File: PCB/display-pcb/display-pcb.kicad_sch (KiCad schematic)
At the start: 7 parts, among them J1 B6B-XH-A, J2 B8B-XH-A, SW1 PTS645SL50-2 LFS, SW2 PTS645SL50-2 LFS, SW3 PTS645SL50-2 LFS, SW4 PTS645SL50-2 LFS, U1 NHD-C12864A1Z

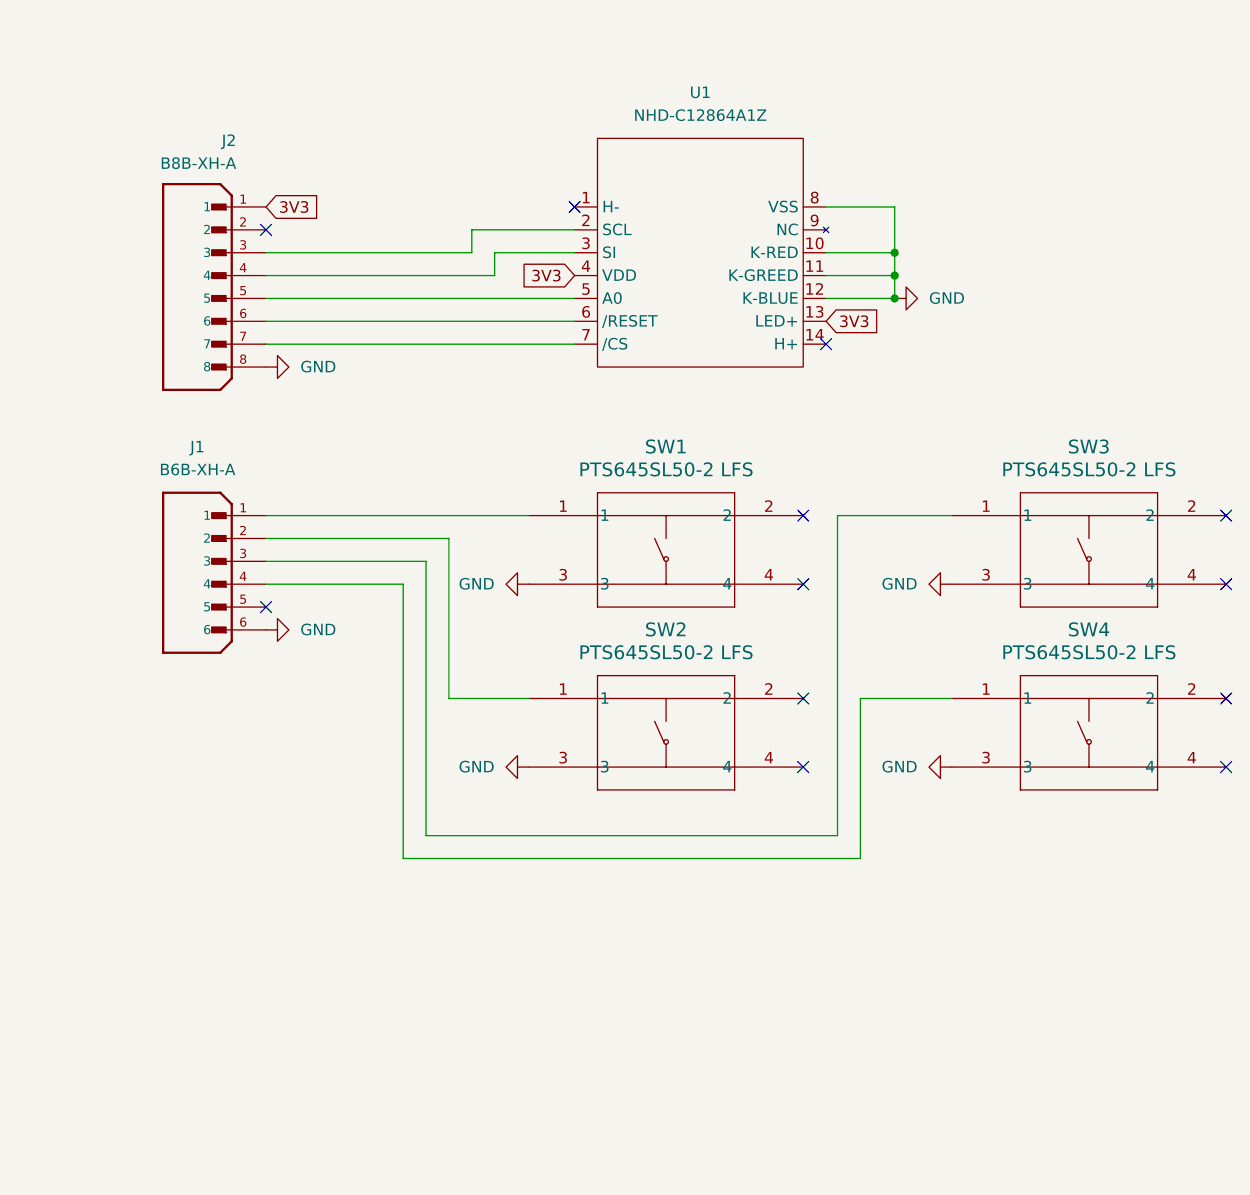
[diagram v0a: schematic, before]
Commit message: changes to display and tube pcb
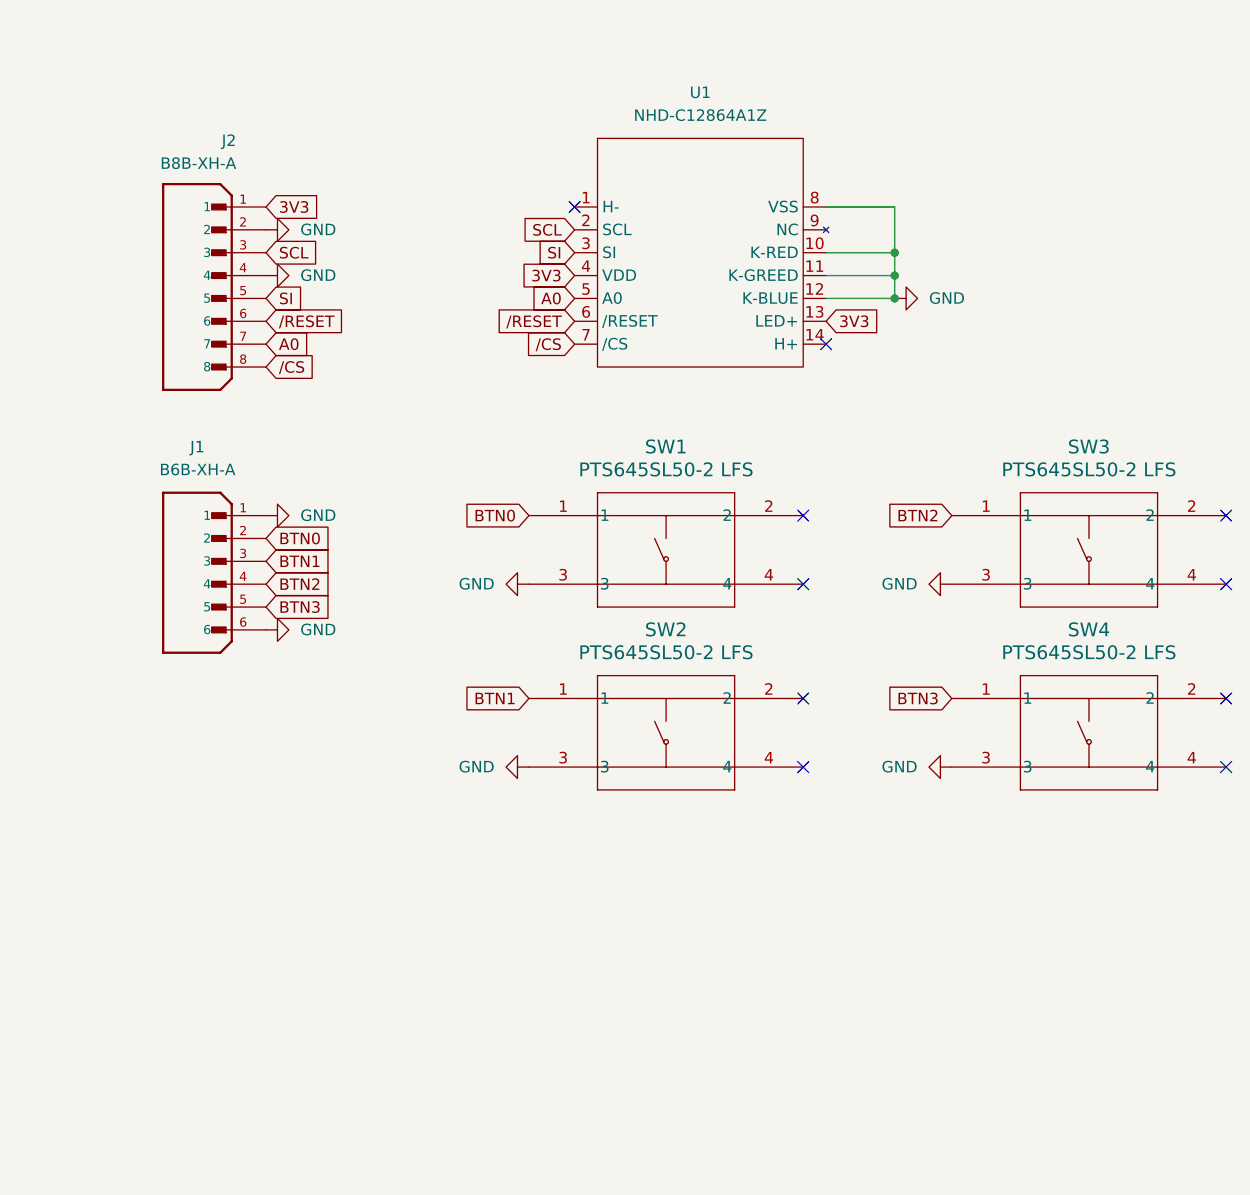
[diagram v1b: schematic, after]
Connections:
- net GND: now also J1.1, J2.2, J2.4; no longer J2.8
- net BTN1: now reaches J1.3
- net BTN1: now also SW2.1; no longer SW3.1
- net BTN0: now reaches SW1.1
- net BTN0: now also J1.2; no longer J1.1
- net BTN2: now reaches J1.4
- net BTN2: now also SW3.1; no longer SW4.1
- net BTN3: now reaches J1.5
- net BTN3: now also SW4.1
- net SCL: now reaches J2.3, U1.2 (SCL)
- net SI: now reaches U1.3 (SI)
- net SI: now also J2.5; no longer J2.4
- net A0: now reaches U1.5 (A0)
- net A0: now also J2.7; no longer J2.5
- net /RESET: now reaches J2.6, U1.6 (/RESET)
- net /CS: now reaches U1.7 (/CS)
- net /CS: now also J2.8; no longer J2.7
- no-connect marks 12 -> 10

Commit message: pcb silkscreens mostly
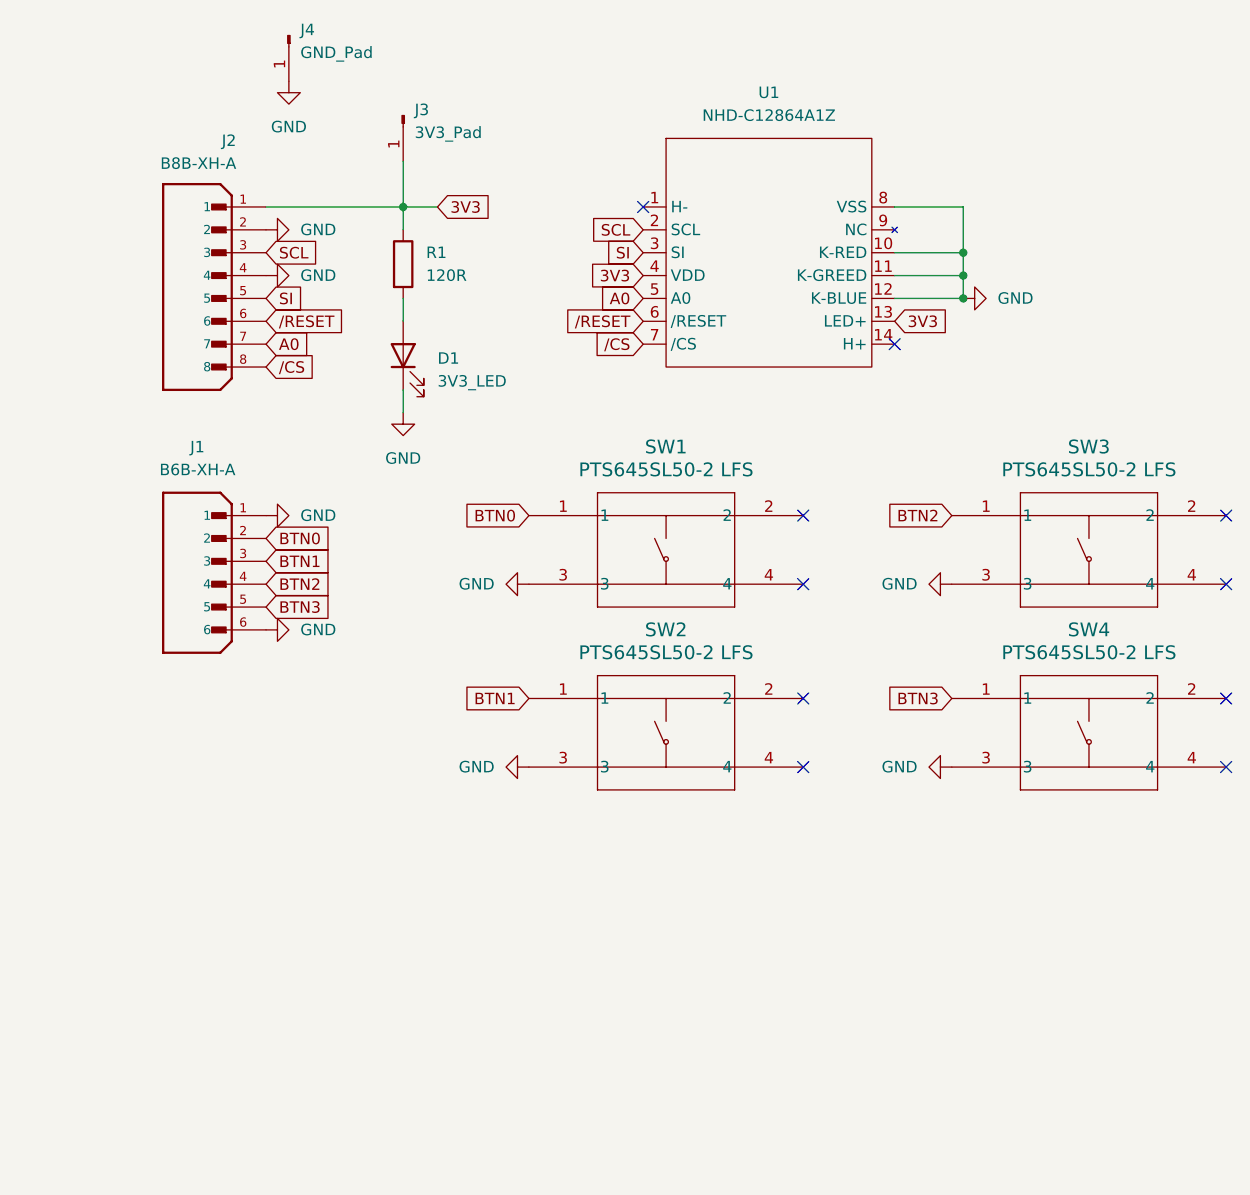
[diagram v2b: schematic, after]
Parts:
- added D1: 3V3_LED, LED_THT:LED_D3.0mm, symbol Device:LED
- added J3: 3V3_Pad, Connector_Wire:SolderWirePad_1x01_SMD_2x4mm, symbol Connector:Conn_01x01_Pin
- added J4: GND_Pad, Connector_Wire:SolderWirePad_1x01_SMD_2x4mm, symbol Connector:Conn_01x01_Pin
- added R1: 120R, 10k-resistor:YAG_MF25_YAG, symbol Device:R
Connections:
- net 3V3: now also J3.1 (Pin_1), R1.1
- net GND: now also D1.1 (K), J4.1 (Pin_1)
- new net: D1.2 (A), R1.2
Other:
- moved on the sheet: U1

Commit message: pcb stuff i forget
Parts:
- removed J3: 3V3_Pad, Connector_Wire:SolderWirePad_1x01_SMD_2x4mm, symbol Connector:Conn_01x01_Pin
- removed J4: GND_Pad, Connector_Wire:SolderWirePad_1x01_SMD_2x4mm, symbol Connector:Conn_01x01_Pin
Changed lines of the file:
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@@
-	(wire
-		(pts
-			(xy 105.41 50.8) (xy 105.41 55.88)
-		)
-		(stroke
-			(width 0)
-			(type default)
-		)
-	)
 	(wire
 		(pts
@@
 	(symbol
 		(lib_id "power:GND")
-		(at 92.71 41.91 0)
-		(unit 1)
-		(exclude_from_sim no)
-		(in_bom yes)
-		(on_board yes)
-		(dnp no)
-		(fields_autoplaced yes)
-		(property "Reference" "#PWR011"
-			(at 92.71 48.26 0)
-			(effects
-				(font
-					(size 1.27 1.27)
-				)
-				(hide yes)
-			)
-		)
-		(property "Value" "GND"
-			(at 92.71 46.99 0)
-			(effects
-				(font
-					(size 1.27 1.27)
-				)
-			)
-		)
-		(property "Footprint" ""
-			(at 92.71 41.91 0)
-			(effects
-				(font
-					(size 1.27 1.27)
-				)
-				(hide yes)
-			)
-		)
-		(property "Datasheet" ""
-			(at 92.71 41.91 0)
-			(effects
-				(font
-					(size 1.27 1.27)
-				)
-				(hide yes)
-			)
-		)
-		(property "Description" "Power symbol creates a global label with name \"GND\" , ground"
-			(at 92.71 41.91 0)
-			(effects
-				(font
-					(size 1.27 1.27)
-				)
-				(hide yes)
-			)
-		)
-		(pin "1"
-		)
-		(instances
-			(project "display-pcb"
-				(path "/35f2d1cd-48fc-4b0c-8241-cdc4ba0a0621"
-					(reference "#PWR011")
-					(unit 1)
-				)
-			)
-		)
-	)
-	(symbol
-		(lib_id "power:GND")
 		(at 166.37 118.11 270)
 		(unit 1)
@@
 	)
 	(symbol
-		(lib_id "Connector:Conn_01x01_Pin")
-		(at 92.71 36.83 270)
-		(unit 1)
-		(exclude_from_sim no)
-		(in_bom yes)
-		(on_board yes)
-		(dnp no)
-		(fields_autoplaced yes)
-		(property "Reference" "J4"
-			(at 93.98 36.1949 90)
-			(effects
-				(font
-					(size 1.27 1.27)
-				)
-				(justify left)
-			)
-		)
-		(property "Value" "GND_Pad"
-			(at 93.98 38.7349 90)
-			(effects
-				(font
-					(size 1.27 1.27)
-				)
-				(justify left)
-			)
-		)
-		(property "Footprint" "Connector_Wire:SolderWirePad_1x01_SMD_2x4mm"
-			(at 92.71 36.83 0)
-			(effects
-				(font
-					(size 1.27 1.27)
-				)
-				(hide yes)
-			)
-		)
-		(property "Datasheet" "~"
-			(at 92.71 36.83 0)
-			(effects
-				(font
-					(size 1.27 1.27)
-				)
-				(hide yes)
-			)
-		)
-		(property "Description" "Generic connector, single row, 01x01, script generated"
-			(at 92.71 36.83 0)
-			(effects
-				(font
-					(size 1.27 1.27)
-				)
-				(hide yes)
-			)
-		)
-		(pin "1"
-		)
-		(instances
-			(project "display-pcb"
-				(path "/35f2d1cd-48fc-4b0c-8241-cdc4ba0a0621"
-					(reference "J4")
-					(unit 1)
-				)
-			)
-		)
-	)
-	(symbol
 		(lib_id "2026-01-20_18-23-47:PTS645SL50-2_LFS")
 		(at 119.38 110.49 0)
@@
 					(unit 1)
 				)
-			)
-		)
-	)
-	(symbol
-		(lib_id "Connector:Conn_01x01_Pin")
-		(at 105.41 45.72 270)
-		(unit 1)
-		(exclude_from_sim no)
-		(in_bom yes)
-		(on_board yes)
-		(dnp no)
-		(fields_autoplaced yes)
-		(property "Reference" "J3"
-			(at 106.68 45.0849 90)
-			(effects
-				(font
-					(size 1.27 1.27)
-				)
-				(justify left)
-			)
-		)
-		(property "Value" "3V3_Pad"
-			(at 106.68 47.6249 90)
-			(effects
-				(font
-					(size 1.27 1.27)
-				)
-				(justify left)
-			)
-		)
-		(property "Footprint" "Connector_Wire:SolderWirePad_1x01_SMD_2x4mm"
-			(at 105.41 45.72 0)
-			(effects
-				(font
-					(size 1.27 1.27)
-				)
-				(hide yes)
-			)
-		)
-		(property "Datasheet" "~"
-			(at 105.41 45.72 0)
-			(effects
-				(font
-					(size 1.27 1.27)
-				)
-				(hide yes)
-			)
-		)
-		(property "Description" "Generic connector, single row, 01x01, script generated"
-			(at 105.41 45.72 0)
-			(effects
-				(font
-					(size 1.27 1.27)
-				)
-				(hide yes)
-			)
-		)
-		(pin "1"
-		)
-		(instances
-			(project ""
-				(path "/35f2d1cd-48fc-4b0c-8241-cdc4ba0a0621"
-					(reference "J3")
-					(unit 1)
-				)

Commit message: PCB updates
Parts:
- added J3: B8B-XH-A, Connector_JST:JST_XH_B8B-XH-A_1x08_P2.50mm_Vertical, symbol B8B-XH-A:B8B-XH-A
- added U2: ~, microsd:pmod-microsd, symbol microsd-2:pmod-microsd
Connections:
- net A0: now also J2.6; no longer J2.7
- net GND: now also J3.2, J3.5, J3.7, U2.5 (GND)
- net /RESET: now also J2.7; no longer J2.6
- new net SD_3V3: J3.8, U2.6 (VCC)
- new net SD_CSn: J3.1, U2.1 (CSn)
- new net SD_MISO: J3.4, U2.3 (MISO/Data0)
- new net SD_MOSI: J3.3, U2.2 (MOSI/Cmd)
- new net SD_SCK: J3.6, U2.4 (SCK)
- no-connect marks 10 -> 16
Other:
- moved on the sheet: J1, J2

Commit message: pcb finishing touches
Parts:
- J2: value B8B-XH-A -> Display_Header
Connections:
- net A0: now also J2.7; no longer J2.6
- net GND: now also J3.4, J3.8; no longer J3.5, J3.7
- net SD_3V3: now also J3.1; no longer J3.8
- net SD_CSn: now also J3.7; no longer J3.1
- net SD_MISO: now also J3.6; no longer J3.4
- net SD_SCK: now also J3.5; no longer J3.6
- net /RESET: now also J2.6; no longer J2.7
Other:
- moved on the sheet: J3
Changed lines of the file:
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@@
 	(wire
 		(pts
-			(xy 86.36 71.12) (xy 90.17 71.12)
+			(xy 160.02 60.96) (xy 167.64 60.96)
 		)
 		(stroke
@@
 	(wire
 		(pts
-			(xy 86.36 68.58) (xy 90.17 68.58)
+			(xy 105.41 55.88) (xy 105.41 58.42)
 		)
 		(stroke
@@
 	(wire
 		(pts
-			(xy 160.02 60.96) (xy 167.64 60.96)
+			(xy 86.36 55.88) (xy 105.41 55.88)
 		)
 		(stroke
@@
 	(wire
 		(pts
-			(xy 105.41 55.88) (xy 105.41 58.42)
+			(xy 86.36 60.96) (xy 90.17 60.96)
 		)
 		(stroke
@@
 	(wire
 		(pts
-			(xy 86.36 55.88) (xy 105.41 55.88)
+			(xy 167.64 55.88) (xy 167.64 60.96)
 		)
 		(stroke
@@
 	(wire
 		(pts
-			(xy 86.36 60.96) (xy 90.17 60.96)
+			(xy 160.02 55.88) (xy 167.64 55.88)
 		)
 		(stroke
@@
 	(wire
 		(pts
-			(xy 167.64 55.88) (xy 167.64 60.96)
+			(xy 86.36 73.66) (xy 90.17 73.66)
 		)
 		(stroke
@@
 	(wire
 		(pts
-			(xy 160.02 55.88) (xy 167.64 55.88)
+			(xy 167.64 63.5) (xy 167.64 66.04)
 		)
 		(stroke
@@
 	(wire
 		(pts
-			(xy 86.36 73.66) (xy 90.17 73.66)
+			(xy 86.36 66.04) (xy 90.17 66.04)
 		)
 		(stroke
@@
 	(wire
 		(pts
-			(xy 167.64 63.5) (xy 167.64 66.04)
+			(xy 105.41 78.74) (xy 105.41 76.2)
 		)
 		(stroke
@@
 	(wire
 		(pts
-			(xy 86.36 66.04) (xy 90.17 66.04)
+			(xy 86.36 63.5) (xy 90.17 63.5)
 		)
 		(stroke
@@
 	(wire
 		(pts
-			(xy 105.41 78.74) (xy 105.41 76.2)
+			(xy 160.02 66.04) (xy 167.64 66.04)
 		)
 		(stroke
@@
 	(wire
 		(pts
-			(xy 86.36 63.5) (xy 90.17 63.5)
+			(xy 167.64 60.96) (xy 167.64 63.5)
 		)
 		(stroke
@@
 	(wire
 		(pts
-			(xy 160.02 66.04) (xy 167.64 66.04)
+			(xy 105.41 55.88) (xy 109.22 55.88)
 		)
 		(stroke
@@
 		)
 	)
-	(wire
-		(pts
-			(xy 167.64 60.96) (xy 167.64 63.5)
-		)
-		(stroke
-			(width 0)
-			(type default)
-		)
-	)
-	(wire
-		(pts
-			(xy 105.41 55.88) (xy 109.22 55.88)
-		)
-		(stroke
-			(width 0)
-			(type default)
-		)
-	)
 	(global_label "A0"
 		(shape input)
-		(at 90.17 68.58 0)
+		(at 86.36 71.12 0)
 		(fields_autoplaced yes)
 		(effects
@@
 		)
 		(property "Intersheetrefs" "${INTERSHEET_REFS}"
-			(at 95.4533 68.58 0)
+			(at 91.6433 71.12 0)
 			(effects
 				(font
@@
 	(global_label "SD_MISO"
 		(shape input)
-		(at 77.47 147.32 0)
+		(at 83.82 144.78 0)
 		(fields_autoplaced yes)
 		(effects
@@
 		)
 		(property "Intersheetrefs" "${INTERSHEET_REFS}"
-			(at 88.4985 147.32 0)
+			(at 94.8485 144.78 0)
 			(effects
 				(font
@@
 	(global_label "SD_MOSI"
 		(shape input)
-		(at 77.47 149.86 0)
+		(at 83.82 137.16 0)
 		(fields_autoplaced yes)
 		(effects
@@
 		)
 		(property "Intersheetrefs" "${INTERSHEET_REFS}"
-			(at 88.4985 149.86 0)
+			(at 94.8485 137.16 0)
 			(effects
 				(font
@@
 	(global_label "SD_SCK"
 		(shape input)
-		(at 77.47 142.24 0)
+		(at 83.82 142.24 0)
 		(fields_autoplaced yes)
 		(effects
@@
 		)
 		(property "Intersheetrefs" "${INTERSHEET_REFS}"
-			(at 87.6518 142.24 0)
+			(at 94.0018 142.24 0)
 			(effects
 				(font
@@
 	(global_label "{slash}RESET"
 		(shape input)
-		(at 90.17 71.12 0)
+		(at 86.36 68.58 0)
 		(fields_autoplaced yes)
 		(effects
@@
 		)
 		(property "Intersheetrefs" "${INTERSHEET_REFS}"
-			(at 100.2308 71.12 0)
+			(at 96.4208 68.58 0)
 			(effects
 				(font
@@
 	(global_label "SD_CSn"
 		(shape input)
-		(at 77.47 154.94 0)
+		(at 83.82 147.32 0)
 		(fields_autoplaced yes)
 		(effects
@@
 		)
 		(property "Intersheetrefs" "${INTERSHEET_REFS}"
-			(at 87.5308 154.94 0)
+			(at 93.8808 147.32 0)
 			(effects
 				(font
@@
 	(global_label "SD_3V3"
 		(shape input)
-		(at 77.47 137.16 0)
+		(at 83.82 132.08 0)
 		(fields_autoplaced yes)
 		(effects
@@
 		)
 		(property "Intersheetrefs" "${INTERSHEET_REFS}"
-			(at 87.4099 137.16 0)
+			(at 93.7599 132.08 0)
 			(effects
 				(font
@@
 			)
 		)
-		(property "Value" "B8B-XH-A"
+		(property "Value" "Display_Header"
 			(at 83.058 51.054 0)
 			(effects
@@
 	(symbol
 		(lib_id "B8B-XH-A:B8B-XH-A")
-		(at 69.85 144.78 180)
+		(at 76.2 142.24 0)
+		(mirror y)
 		(unit 1)
 		(exclude_from_sim no)
@@
 		(dnp no)
 		(property "Reference" "J3"
-			(at 74.168 162.306 0)
+			(at 80.518 124.714 0)
 			(effects
 				(font
@@
 		)
 		(property "Value" "B8B-XH-A"
-			(at 74.168 159.766 0)
+			(at 80.518 127.254 0)
 			(effects
 				(font
@@
 		)
 		(property "Footprint" "Connector_JST:JST_XH_B8B-XH-A_1x08_P2.50mm_Vertical"
-			(at 69.85 144.78 0)
+			(at 76.2 142.24 0)
 			(effects
 				(font
@@
 		)
 		(property "Datasheet" ""
-			(at 69.85 144.78 0)
+			(at 76.2 142.24 0)
 			(effects
 				(font
@@
 		)
 		(property "Description" ""
-			(at 69.85 144.78 0)
+			(at 76.2 142.24 0)
 			(effects
 				(font
@@
 		)
 		(property "PARTREV" "7/4/21"
-			(at 69.85 144.78 0)
+			(at 76.2 142.24 0)
 			(effects
 				(font
@@
 		)
 		(property "STANDARD" "Manufacturer Recommendations"
-			(at 69.85 144.78 0)
+			(at 76.2 142.24 0)
 			(effects
 				(font
@@
 		)
 		(property "MAXIMUM_PACKAGE_HEIGHT" "7.00 mm"
-			(at 69.85 144.78 0)
+			(at 76.2 142.24 0)
 			(effects
 				(font
@@
 		)
 		(property "MANUFACTURER" "JST"
-			(at 69.85 144.78 0)
+			(at 76.2 142.24 0)
 			(effects
 				(font
@@
 	(symbol
 		(lib_id "power:GND")
-		(at 77.47 152.4 90)
+		(at 83.82 149.86 90)
 		(unit 1)
 		(exclude_from_sim no)
@@
 		(fields_autoplaced yes)
 		(property "Reference" "#PWR013"
-			(at 83.82 152.4 0)
+			(at 90.17 149.86 0)
 			(effects
 				(font
@@
 		)
 		(property "Value" "GND"
-			(at 81.28 152.3999 90)
+			(at 87.63 149.8599 90)
 			(effects
 				(font
@@
 		)
 		(property "Footprint" ""
-			(at 77.47 152.4 0)
+			(at 83.82 149.86 0)
 			(effects
 				(font
@@
 		)
 		(property "Datasheet" ""
-			(at 77.47 152.4 0)
+			(at 83.82 149.86 0)
 			(effects
 				(font
@@
 		)
 		(property "Description" "Power symbol creates a global label with name \"GND\" , ground"
-			(at 77.47 152.4 0)
+			(at 83.82 149.86 0)
 			(effects
 				(font
@@
 	(symbol
 		(lib_id "power:GND")
-		(at 77.47 139.7 90)
+		(at 83.82 134.62 90)
 		(unit 1)
 		(exclude_from_sim no)
@@
 		(fields_autoplaced yes)
 		(property "Reference" "#PWR014"
-			(at 83.82 139.7 0)
+			(at 90.17 134.62 0)
 			(effects
 				(font
@@
 		)
 		(property "Value" "GND"
-			(at 81.28 139.6999 90)
+			(at 87.63 134.6199 90)
 			(effects
 				(font
@@
 		)
 		(property "Footprint" ""
-			(at 77.47 139.7 0)
+			(at 83.82 134.62 0)
 			(effects
 				(font
@@
 		)
 		(property "Datasheet" ""
-			(at 77.47 139.7 0)
+			(at 83.82 134.62 0)
 			(effects
 				(font
@@
 		)
 		(property "Description" "Power symbol creates a global label with name \"GND\" , ground"
-			(at 77.47 139.7 0)
+			(at 83.82 134.62 0)
 			(effects
 				(font
@@
 	(symbol
 		(lib_id "power:GND")
-		(at 77.47 144.78 90)
+		(at 83.82 139.7 90)
 		(unit 1)
 		(exclude_from_sim no)
@@
 		(fields_autoplaced yes)
 		(property "Reference" "#PWR011"
-			(at 83.82 144.78 0)
+			(at 90.17 139.7 0)
 			(effects
 				(font
@@
 		)
 		(property "Value" "GND"
-			(at 81.28 144.7799 90)
+			(at 87.63 139.6999 90)
 			(effects
 				(font
@@
 		)
 		(property "Footprint" ""
-			(at 77.47 144.78 0)
+			(at 83.82 139.7 0)
 			(effects
 				(font
@@
 		)
 		(property "Datasheet" ""
-			(at 77.47 144.78 0)
+			(at 83.82 139.7 0)
 			(effects
 				(font
@@
 		)
 		(property "Description" "Power symbol creates a global label with name \"GND\" , ground"
-			(at 77.47 144.78 0)
-			(effects
-				(font
+			(at 83.82 139.7 0)
+			(effects
+				(font

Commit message: gerbs
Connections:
- net A0: now also J2.6; no longer J2.7
- net /RESET: now also J2.7; no longer J2.6
